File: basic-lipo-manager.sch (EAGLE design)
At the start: 23 parts, among them U2 MCP73831

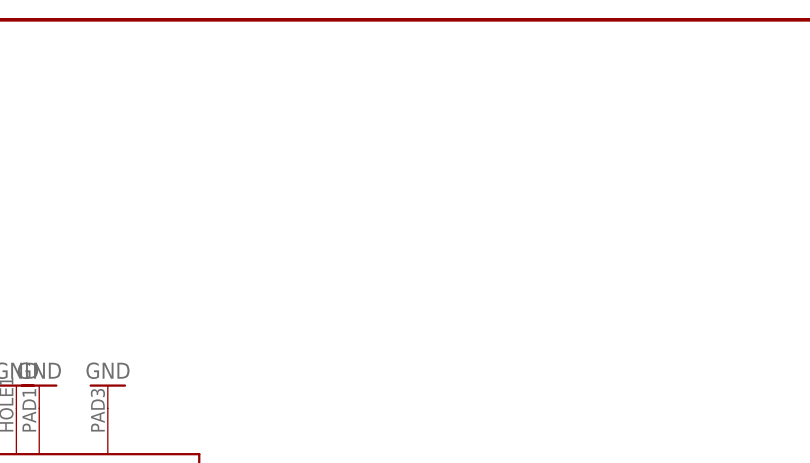
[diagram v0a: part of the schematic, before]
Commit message: label edits, fiducials added
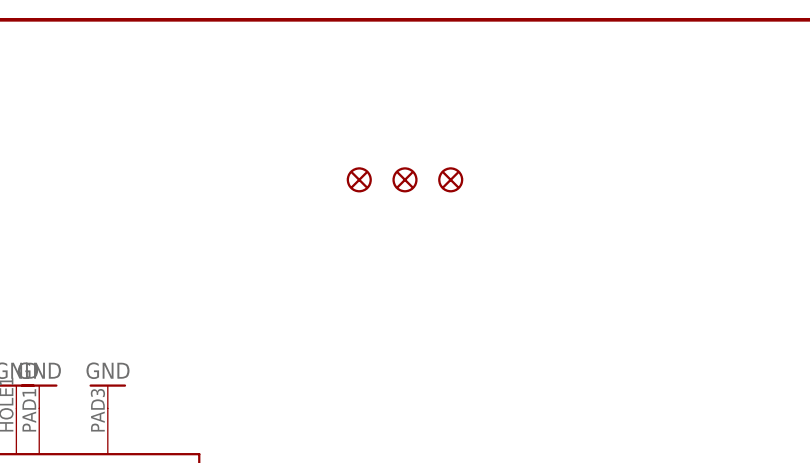
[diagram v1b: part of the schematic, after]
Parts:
- added FID1, FID2, FID3: FIDUCIAL1X2, SparkFun-Aesthetics:FIDUCIAL1X2
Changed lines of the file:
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@@
 <part name="JP4" library="SparkFun-Connectors" deviceset="M04" device="PTH"/>
 <part name="JP5" library="SparkFun-Connectors" deviceset="M02" device="PTH"/>
+<part name="FID1" library="SparkFun-Aesthetics" deviceset="FIDUCIAL" device="1X2"/>
+<part name="FID2" library="SparkFun-Aesthetics" deviceset="FIDUCIAL" device="1X2"/>
+<part name="FID3" library="SparkFun-Aesthetics" deviceset="FIDUCIAL" device="1X2"/>
 </parts>
 <sheets>
@@
 </instance>
 <instance part="JP5" gate="G$1" x="76.2" y="88.9" rot="R180"/>
+<instance part="FID1" gate="G$1" x="78.74" y="167.64"/>
+<instance part="FID2" gate="G$1" x="83.82" y="167.64"/>
+<instance part="FID3" gate="G$1" x="88.9" y="167.64"/>
 </instances>
 <busses>
